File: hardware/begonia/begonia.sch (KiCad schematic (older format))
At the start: 11 parts, among them J1 NEIGHBOR1, J2 NEIGHBOR2, J7 BONUS_ROW, P1 POGOPINS, SW1 SPST

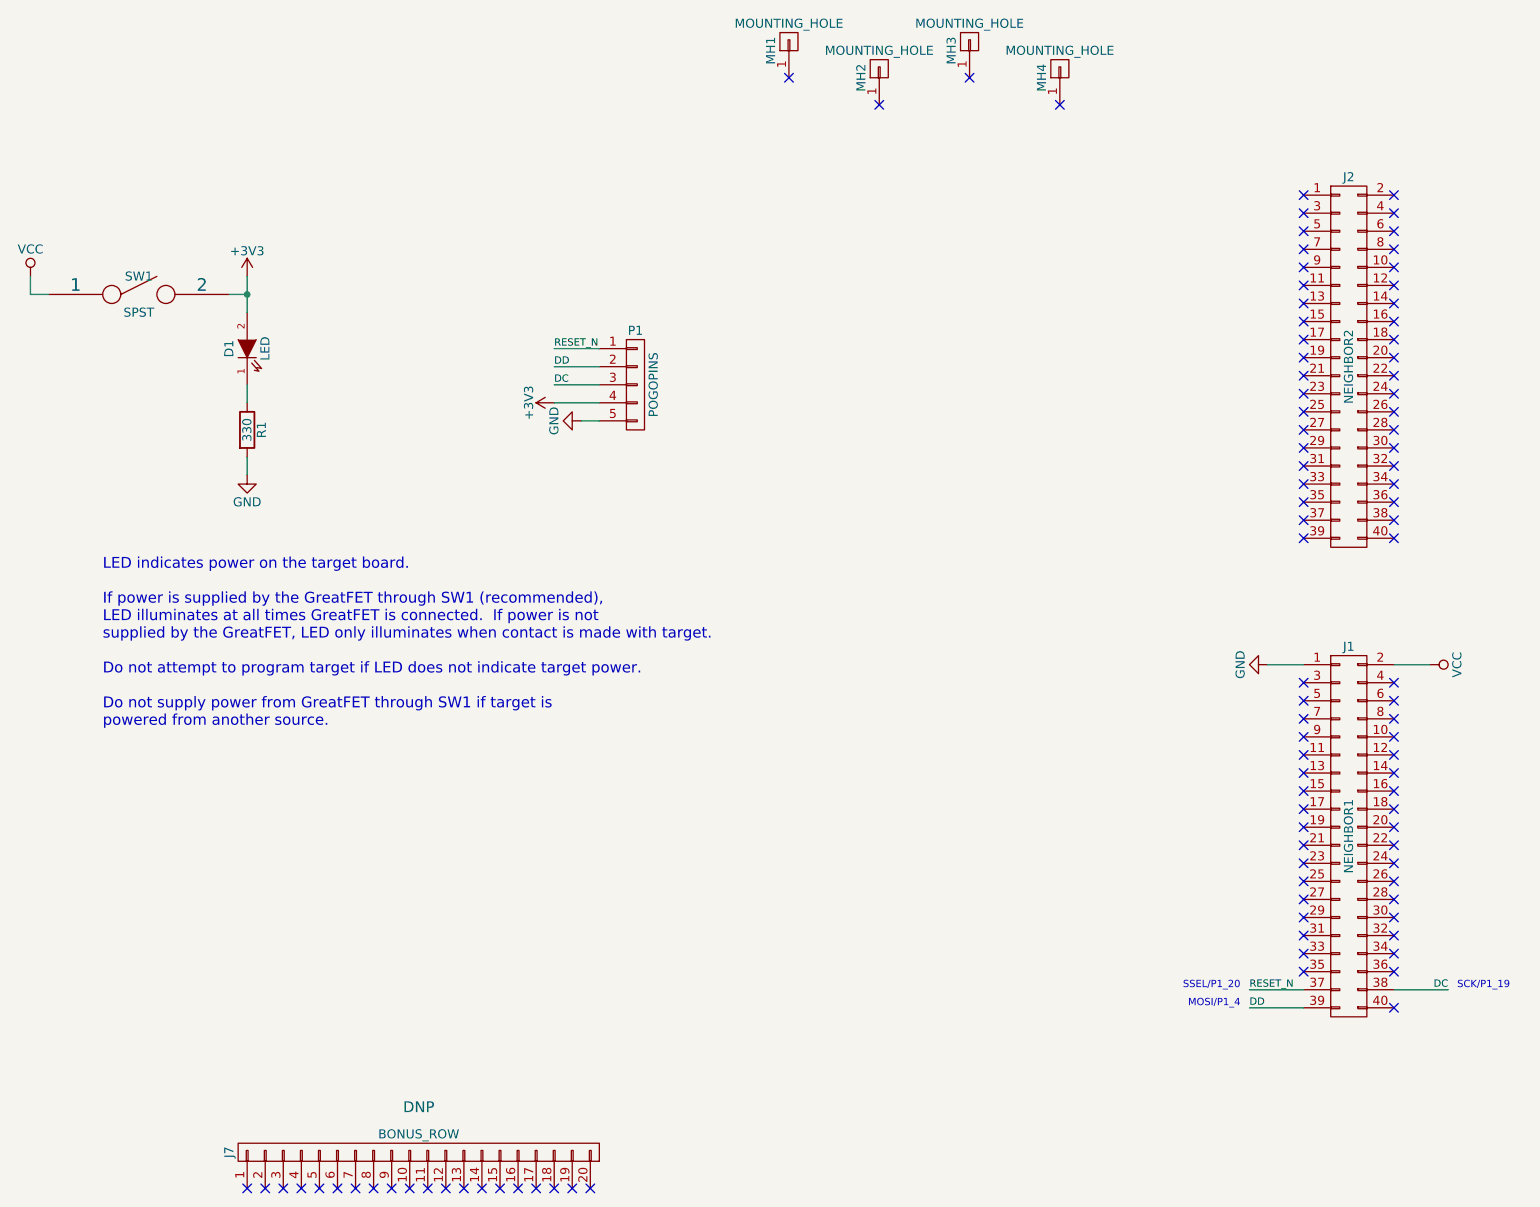
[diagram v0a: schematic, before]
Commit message: begonia: added alternative pins for RESET_N signal
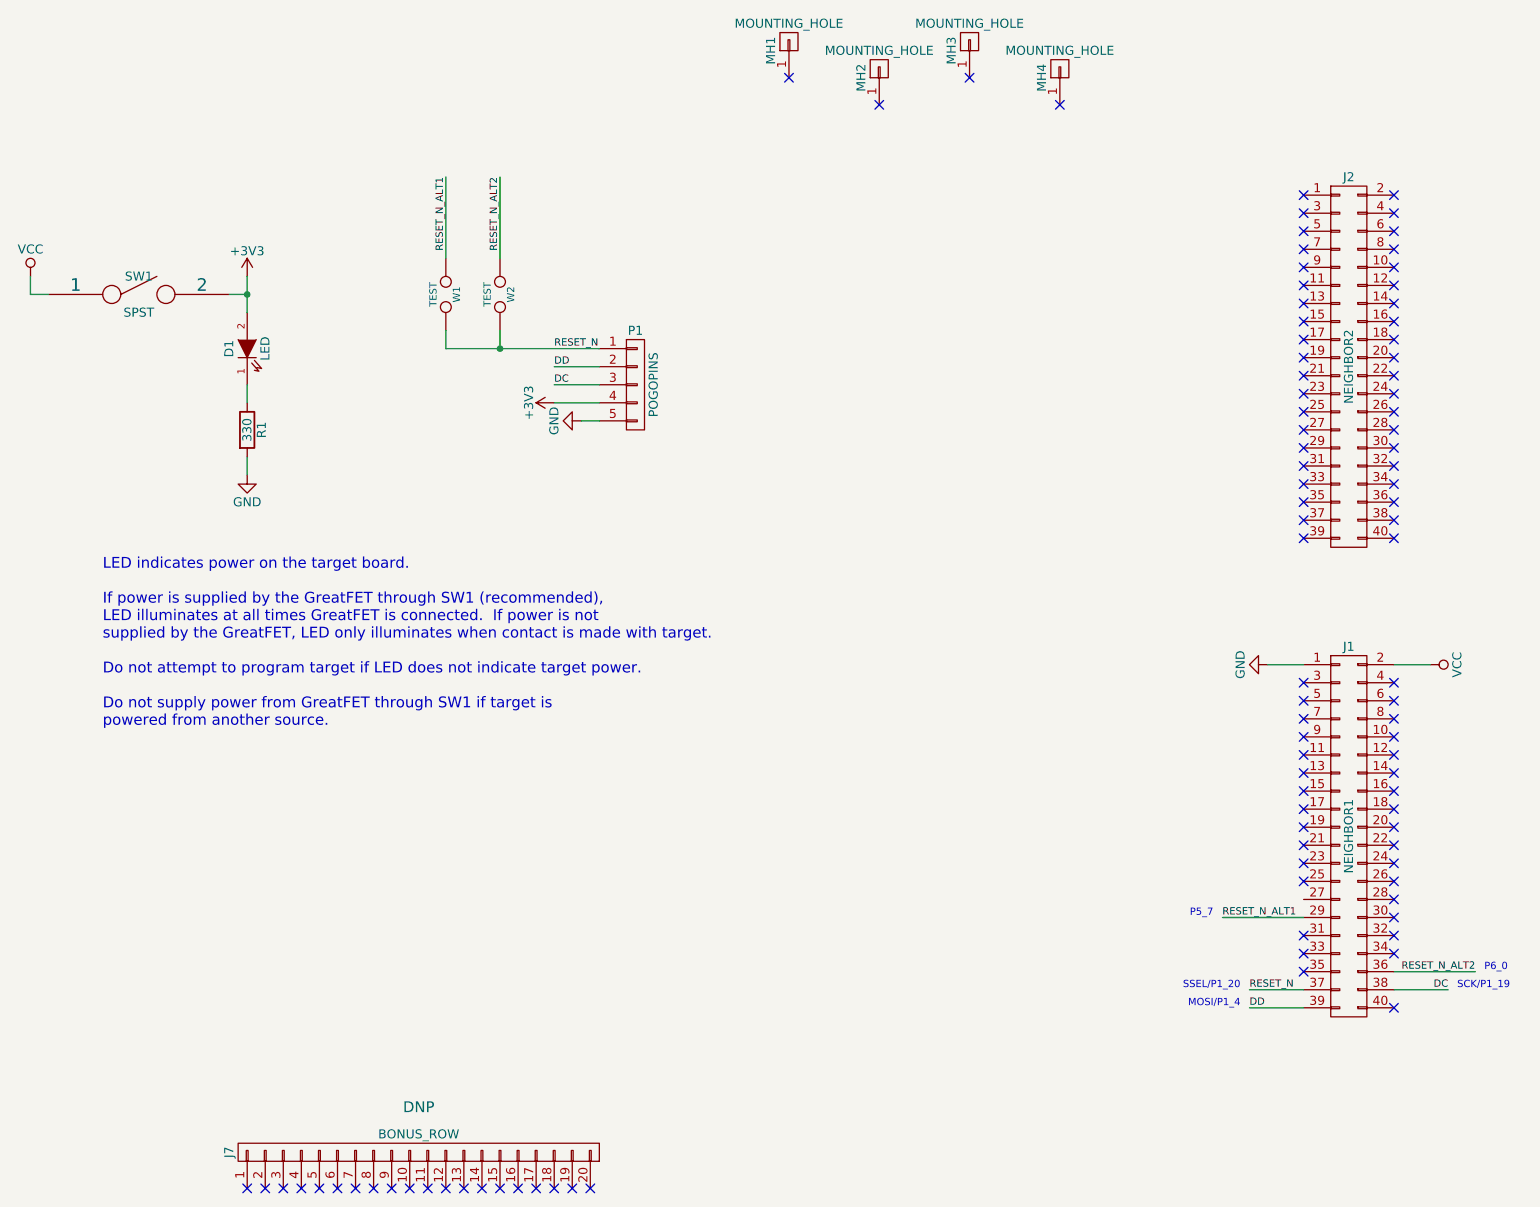
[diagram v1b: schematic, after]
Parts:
- added W1, W2: TEST, gsg-modules:0603-JUMPER, symbol TEST
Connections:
- net RESET_N: now also W1.2, W2.2
- net RESET_N_ALT1: now reaches J1.29 (P29)
- net RESET_N_ALT1: now also W1.1
- net RESET_N_ALT2: now reaches J1.36 (P36)
- net RESET_N_ALT2: now also W2.1
- no-connect marks 99 -> 96
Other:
- note added: "P5_7"
- note added: "P6_0"
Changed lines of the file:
@@
 $EndComp
 $Comp
-L GND #PWR01
+L GND #PWR6
 U 1 1 55EAECD0
 P 8700 4300
-F 0 "#PWR01" H 8700 4050 50  0001 C CNN
+F 0 "#PWR6" H 8700 4050 50  0001 C CNN
 F 1 "GND" H 8700 4150 50  0000 C CNN
 F 2 "" H 8700 4300 60  0000 C CNN
@@
 $EndComp
 $Comp
-L VCC #PWR02
+L VCC #PWR7
 U 1 1 55EAF03E
 P 9600 4300
-F 0 "#PWR02" H 9600 4150 50  0001 C CNN
+F 0 "#PWR7" H 9600 4150 50  0001 C CNN
 F 1 "VCC" H 9600 4450 50  0000 C CNN
 F 2 "" H 9600 4300 60  0000 C CNN
@@
 LED indicates power on the target board.\n\nIf power is supplied by the GreatFET through SW1 (recommended),\nLED illuminates at all times GreatFET is connected.  If power is not\nsupplied by the GreatFET, LED only illuminates when contact is made with target.\n\nDo not attempt to program target if LED does not indicate target power.\n\nDo not supply power from GreatFET through SW1 if target is\npowered from another source.
 Wire Wire Line
-	4750 2550 5000 2550
+	4150 2550 5000 2550
 Wire Wire Line
 	4750 2650 5000 2650
@@
 $EndComp
 $Comp
-L +3V3 #PWR03
+L +3V3 #PWR3
 U 1 1 5605043F
 P 4750 2850
-F 0 "#PWR03" H 4750 2700 50  0001 C CNN
+F 0 "#PWR3" H 4750 2700 50  0001 C CNN
 F 1 "+3V3" H 4750 2990 50  0000 C CNN
 F 2 "" H 4750 2850 60  0000 C CNN
@@
 $EndComp
 $Comp
-L GND #PWR04
+L GND #PWR4
 U 1 1 56050471
 P 4900 2950
-F 0 "#PWR04" H 4900 2700 50  0001 C CNN
+F 0 "#PWR4" H 4900 2700 50  0001 C CNN
 F 1 "GND" H 4900 2800 50  0000 C CNN
 F 2 "" H 4900 2950 60  0000 C CNN
@@
 $EndComp
 $Comp
-L GND #PWR05
+L GND #PWR5
 U 1 1 56050EAD
 P 3050 3250
-F 0 "#PWR05" H 3050 3000 50  0001 C CNN
+F 0 "#PWR5" H 3050 3000 50  0001 C CNN
 F 1 "GND" H 3050 3100 50  0000 C CNN
 F 2 "" H 3050 3250 60  0000 C CNN
@@
 $EndComp
 $Comp
-L +3V3 #PWR06
+L +3V3 #PWR2
 U 1 1 56050F23
 P 3050 2150
-F 0 "#PWR06" H 3050 2000 50  0001 C CNN
+F 0 "#PWR2" H 3050 2000 50  0001 C CNN
 F 1 "+3V3" H 3050 2290 50  0000 C CNN
 F 2 "" H 3050 2150 60  0000 C CNN
@@
 Connection ~ 3050 2250
 $Comp
-L VCC #PWR07
+L VCC #PWR1
 U 1 1 5605133F
 P 1850 2150
-F 0 "#PWR07" H 1850 2000 50  0001 C CNN
+F 0 "#PWR1" H 1850 2000 50  0001 C CNN
 F 1 "VCC" H 1850 2300 50  0000 C CNN
 F 2 "" H 1850 2150 60  0000 C CNN
@@
 NoConn ~ 8900 5400
 NoConn ~ 8900 5500
-NoConn ~ 8900 5600
-NoConn ~ 8900 5700
 NoConn ~ 8900 5800
 NoConn ~ 8900 5900
 NoConn ~ 8900 6000
 NoConn ~ 9400 6200
-NoConn ~ 9400 6000
 NoConn ~ 9400 5900
 NoConn ~ 9400 5800
@@
 NoConn ~ 9400 5500
 NoConn ~ 9400 5400
+Text Notes 8400 5700 2    40   ~ 0
+P5_7
+Text Notes 9900 6000 0    40   ~ 0
+P6_0
+Wire Wire Line
+	8450 5700 8900 5700
+Text Label 8450 5700 0    40   ~ 0
+RESET_N_ALT1
+Text Label 9850 6000 2    40   ~ 0
+RESET_N_ALT2
+Wire Wire Line
+	9850 6000 9400 6000
+$Comp
+L TEST W2
+U 1 1 56086936
+P 4450 2250
+F 0 "W2" H 4450 2310 40  0000 C CNN
+F 1 "TEST" H 4450 2180 40  0000 C CNN
+F 2 "gsg-modules:0603-JUMPER" H 4450 2250 60  0001 C CNN
+F 3 "" H 4450 2250 60  0000 C CNN
+	1    4450 2250
+	0    1    1    0
+$EndComp
+$Comp
+L TEST W1
+U 1 1 56086AFD
+P 4150 2250
+F 0 "W1" H 4150 2310 40  0000 C CNN
+F 1 "TEST" H 4150 2180 40  0000 C CNN
+F 2 "gsg-modules:0603-JUMPER" H 4150 2250 60  0001 C CNN
+F 3 "" H 4150 2250 60  0000 C CNN
+	1    4150 2250
+	0    1    1    0
+$EndComp
+Wire Wire Line
+	4150 2450 4150 2550
+Wire Wire Line
+	4450 2450 4450 2550
+Connection ~ 4450 2550
+Wire Wire Line
+	4450 1600 4450 2050
+Wire Wire Line
+	4150 1600 4150 2050
+Text Label 4150 1600 3    40   ~ 0
+RESET_N_ALT1
+Text Label 4450 1600 3    40   ~ 0
+RESET_N_ALT2
 $EndSCHEMATC

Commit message: azalea: renamed MCU_XTAL
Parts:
- J1, J2: Description (none) -> CONN RCPT .100\" 40POS DUAL-ROW STACKING GOLD; Manufacturer (none) -> Samtec; Part Number (none) -> SSQ-120-23-G-D
- J7: Description (none) -> CONN RCPT .100\" 20POS SINGLE-ROW STACKING GOLD; Manufacturer (none) -> Samtec; Part Number (none) -> SSQ-120-23-G-S
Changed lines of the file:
@@
 F 2 "gsg-modules:HEADER-2x20" H 9150 1700 60  0001 C CNN
 F 3 "" H 9150 1700 60  0000 C CNN
+F 4 "Samtec" H 9150 2650 60  0001 C CNN "Manufacturer"
+F 5 "SSQ-120-23-G-D" H 9150 2650 60  0001 C CNN "Part Number"
+F 6 "CONN RCPT .100\" 40POS DUAL-ROW STACKING GOLD" H 9150 2650 60  0001 C CNN "Description"
 	1    9150 2650
 	1    0    0    -1
@@
 F 2 "gsg-modules:HEADER-2x20" H 9150 4300 60  0001 C CNN
 F 3 "" H 9150 4300 60  0000 C CNN
+F 4 "Samtec" H 9150 5250 60  0001 C CNN "Manufacturer"
+F 5 "SSQ-120-23-G-D" H 9150 5250 60  0001 C CNN "Part Number"
+F 6 "CONN RCPT .100\" 40POS DUAL-ROW STACKING GOLD" H 9150 5250 60  0001 C CNN "Description"
 	1    9150 5250
 	1    0    0    -1
@@
 F 2 "gsg-modules:HEADER-1x20" H 4000 7000 60  0001 C CNN
 F 3 "" H 4000 7000 60  0000 C CNN
-F 4 "DNP" V 4250 7000 60  0000 C CNN "Note"
+F 4 "Samtec" H 4000 7000 60  0001 C CNN "Manufacturer"
+F 5 "SSQ-120-23-G-S" H 4000 7000 60  0001 C CNN "Part Number"
+F 6 "CONN RCPT .100\" 20POS SINGLE-ROW STACKING GOLD" H 4000 7000 60  0001 C CNN "Description"
+F 7 "DNP" V 4250 7000 60  0000 C CNN "Note"
 	1    4000 7000
 	0    -1   -1   0

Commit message: neighbors: alternate header selection
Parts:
- J1, J2: Note (none) -> Alternate: https://www.adafruit.com/products/2223
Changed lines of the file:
@@
 F 5 "SSQ-120-23-G-D" H 9150 2650 60  0001 C CNN "Part Number"
 F 6 "CONN RCPT .100\" 40POS DUAL-ROW STACKING GOLD" H 9150 2650 60  0001 C CNN "Description"
+F 7 "Alternate: https://www.adafruit.com/products/2223" H 9150 2650 60  0001 C CNN "Note"
 	1    9150 2650
 	1    0    0    -1
@@
 F 5 "SSQ-120-23-G-D" H 9150 5250 60  0001 C CNN "Part Number"
 F 6 "CONN RCPT .100\" 40POS DUAL-ROW STACKING GOLD" H 9150 5250 60  0001 C CNN "Description"
+F 7 "Alternate: https://www.adafruit.com/products/2223" H 9150 5250 60  0001 C CNN "Note"
 	1    9150 5250
 	1    0    0    -1

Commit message: begonia: designated solder jumpers DNP
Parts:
- W1, W2: Note (none) -> DNP
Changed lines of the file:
@@
 F 2 "gsg-modules:0603-JUMPER" H 4450 2250 60  0001 C CNN
 F 3 "" H 4450 2250 60  0000 C CNN
+F 4 "DNP" H 4450 2250 60  0001 C CNN "Note"
 	1    4450 2250
 	0    1    1    0
@@
 F 2 "gsg-modules:0603-JUMPER" H 4150 2250 60  0001 C CNN
 F 3 "" H 4150 2250 60  0000 C CNN
+F 4 "DNP" H 4150 2250 60  0001 C CNN "Note"
 	1    4150 2250
 	0    1    1    0
